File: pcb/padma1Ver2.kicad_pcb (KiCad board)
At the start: 2 copper layers, 33 x 68.6 mm, 15 parts, among them SW1 SPST

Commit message: added basic Pcb File
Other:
- board text added: "Padma1Ver2 - KSRMCE Kunchala Anil"
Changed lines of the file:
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@@
     (area 143.459999 81.229999 176.580001 149.910001)
     (thickness 1.6)
-    (drawings 7)
+    (drawings 8)
     (tracks 165)
     (zones 0)
@@
       (net 40 "Net-(R3-Pad1)"))
   )
+  (gr_text "Padma1Ver2 -  KSRMCE\nKunchala Anil" (at 166.37 83.185) (layer F.SilkS)
+    (effects (font (size 1 1) (thickness 0.25)))
+  )
   (gr_line (start 143.51 81.28) (end 143.51 82.55) (angle 90) (layer Edge.Cuts) (width 0.1))

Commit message: added ConfigJson Description file
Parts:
- D3: value LED_RCBG -> LED_RGB
- moved 10k1 3.17 mm to (150.5, 87.6)
- renumbered DTH1 to DTH, LDR1 to LDR, MOIS1 to SMS
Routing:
- net Net-(10k1-Pad2): track 39.1 -> 82.9 mm, vias 1 -> 3
- net Net-(10k1-Pad1): track 31.9 -> 61.9 mm
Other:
- board text added: "Padma1Ver2 - Innovation Lab"
- board text removed: "Padma1Ver2 - KSRMCE Kunchala Anil"
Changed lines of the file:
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@@
     (thickness 1.6)
     (drawings 8)
-    (tracks 165)
+    (tracks 186)
     (zones 0)
     (modules 15)
@@
     (visible_elements FFFFFF7F)
     (pcbplotparams
-      (layerselection 0x00030_80000001)
+      (layerselection 0x010f0_80000001)
       (usegerberextensions false)
       (excludeedgelayer true)
@@
       (outputformat 1)
       (mirror false)
-      (drillshape 1)
+      (drillshape 0)
       (scaleselection 1)
       (outputdirectory ""))
@@
   )
   (module Resistors_ThroughHole:Resistor_Horizontal_RM10mm placed (layer F.Cu)
-    (at 148.59 85.09)
+    (at 150.495 87.63)
     (descr "Resistor, Axial,  RM 10mm, 1/3W")
     (tags "Resistor Axial RM 10mm 1/3W")
@@
       (effects (font (size 1 1) (thickness 0.15)))
     )
-    (fp_text value LED_RCBG (at 3.175 1.27 540) (layer F.Fab)
+    (fp_text value LED_RGB (at 3.175 1.27 360) (layer F.Fab)
       (effects (font (size 1 1) (thickness 0.15)))
     )
@@
     (descr "Through hole pin header")
     (tags "pin header")
-    (fp_text reference DTH1 (at 3.175 3.81 90) (layer F.SilkS)
+    (fp_text reference DTH (at 3.175 3.81 90) (layer F.SilkS)
       (effects (font (size 1 1) (thickness 0.15)))
     )
@@
     (descr "Through hole pin header")
     (tags "pin header")
-    (fp_text reference LDR1 (at -2.54 3.81 270) (layer F.SilkS)
+    (fp_text reference LDR (at -2.54 3.81 270) (layer F.SilkS)
       (effects (font (size 1 1) (thickness 0.15)))
     )
@@
     (descr "Through hole pin header")
     (tags "pin header")
-    (fp_text reference MOIS1 (at 2.54 3.175 90) (layer F.SilkS)
+    (fp_text reference SMS (at 2.54 3.175 90) (layer F.SilkS)
       (effects (font (size 1 1) (thickness 0.15)))
     )
@@
       (net 40 "Net-(R3-Pad1)"))
   )
-  (gr_text "Padma1Ver2 -  KSRMCE\nKunchala Anil" (at 166.37 83.185) (layer F.SilkS)
+  (gr_text "Padma1Ver2 -  Innovation Lab\n" (at 162.56 82.55) (layer F.SilkS)
     (effects (font (size 1 1) (thickness 0.25)))
   )
@@
   (segment (start 170.18 106.045) (end 170.815 106.68) (width 0.25) (layer B.Cu) (net 2) (status 80000))
   (segment (start 170.815 106.68) (end 171.45 106.68) (width 0.25) (layer B.Cu) (net 2) (status 80000))
+  (segment (start 150.495 87.63) (end 151.13 88.265) (width 0.25) (layer F.Cu) (net 3) (status 80000))
+  (segment (start 151.13 88.265) (end 151.13 89.535) (width 0.25) (layer F.Cu) (net 3) (status 80000))
+  (segment (start 151.13 89.535) (end 153.035 91.44) (width 0.25) (layer F.Cu) (net 3) (status 80000))
+  (segment (start 153.035 91.44) (end 153.035 93.345) (width 0.25) (layer F.Cu) (net 3) (status 80000))
+  (segment (start 153.035 93.345) (end 154.305 94.615) (width 0.25) (layer F.Cu) (net 3) (status 80000))
+  (segment (start 154.305 94.615) (end 154.305 111.76) (width 0.25) (layer F.Cu) (net 3) (status 80000))
+  (segment (start 154.305 111.76) (end 156.845 111.76) (width 0.25) (layer F.Cu) (net 3) (status 80000))
+  (segment (start 156.845 111.76) (end 158.115 113.03) (width 0.25) (layer F.Cu) (net 3) (status 80000))
   (segment (start 148.59 85.09) (end 154.305 90.805) (width 0.25) (layer F.Cu) (net 3) (status 80000))
   (segment (start 154.305 90.805) (end 154.305 92.71) (width 0.25) (layer F.Cu) (net 3) (status 80000))
@@
   (segment (start 156.845 109.22) (end 158.115 110.49) (width 0.25) (layer F.Cu) (net 3) (status 80000))
   (segment (start 158.115 110.49) (end 158.115 113.03) (width 0.25) (layer F.Cu) (net 3) (status 80000))
+  (segment (start 168.275 114.935) (end 168.91 115.57) (width 0.25) (layer B.Cu) (net 4) (status 80000))
+  (segment (start 168.91 115.57) (end 173.355 115.57) (width 0.25) (layer B.Cu) (net 4) (status 80000))
+  (segment (start 173.355 115.57) (end 176.53 112.395) (width 0.25) (layer B.Cu) (net 4) (status 80000))
+  (via (at 176.53 112.395) (size 0.6) (layers F.Cu B.Cu) (net 4) (status 80000))
+  (segment (start 176.53 112.395) (end 175.895 111.76) (width 0.25) (layer F.Cu) (net 4) (status 80000))
+  (segment (start 175.895 111.76) (end 175.895 99.06) (width 0.25) (layer F.Cu) (net 4) (status 80000))
+  (via (at 175.895 99.06) (size 0.6) (layers F.Cu B.Cu) (net 4) (status 80000))
+  (segment (start 175.895 99.06) (end 174.625 97.79) (width 0.25) (layer B.Cu) (net 4) (status 80000))
+  (segment (start 174.625 97.79) (end 174.625 97.155) (width 0.25) (layer B.Cu) (net 4) (status 80000))
+  (segment (start 174.625 97.155) (end 170.815 97.155) (width 0.25) (layer B.Cu) (net 4) (status 80000))
+  (segment (start 170.815 97.155) (end 165.1 91.44) (width 0.25) (layer B.Cu) (net 4) (status 80000))
+  (segment (start 165.1 91.44) (end 164.465 91.44) (width 0.25) (layer B.Cu) (net 4) (status 80000))
+  (segment (start 164.465 91.44) (end 160.655 87.63) (width 0.25) (layer B.Cu) (net 4) (status 80000))
   (segment (start 168.275 114.935) (end 167.005 116.205) (width 0.25) (layer B.Cu) (net 4) (status 80000))
   (segment (start 167.005 116.205) (end 166.37 116.205) (width 0.25) (layer B.Cu) (net 4) (status 80000))

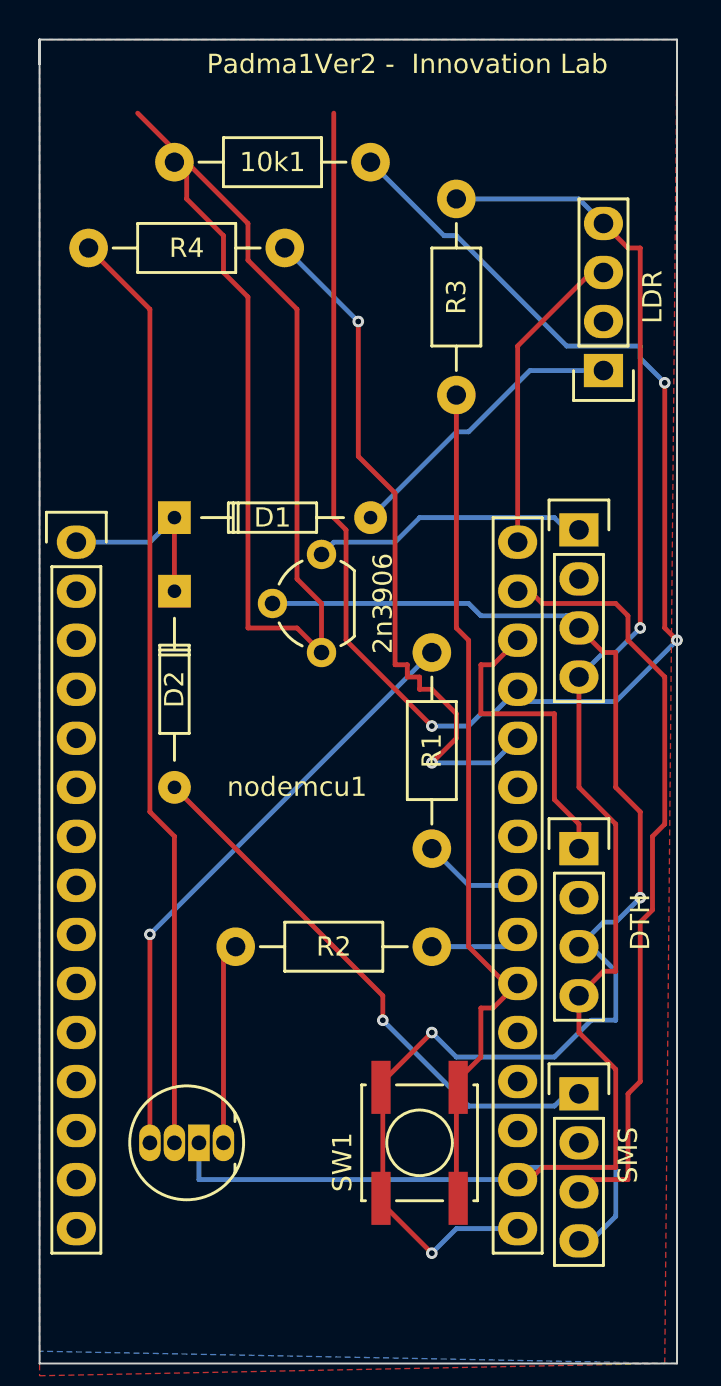
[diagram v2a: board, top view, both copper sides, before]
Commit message: added random clientid generator
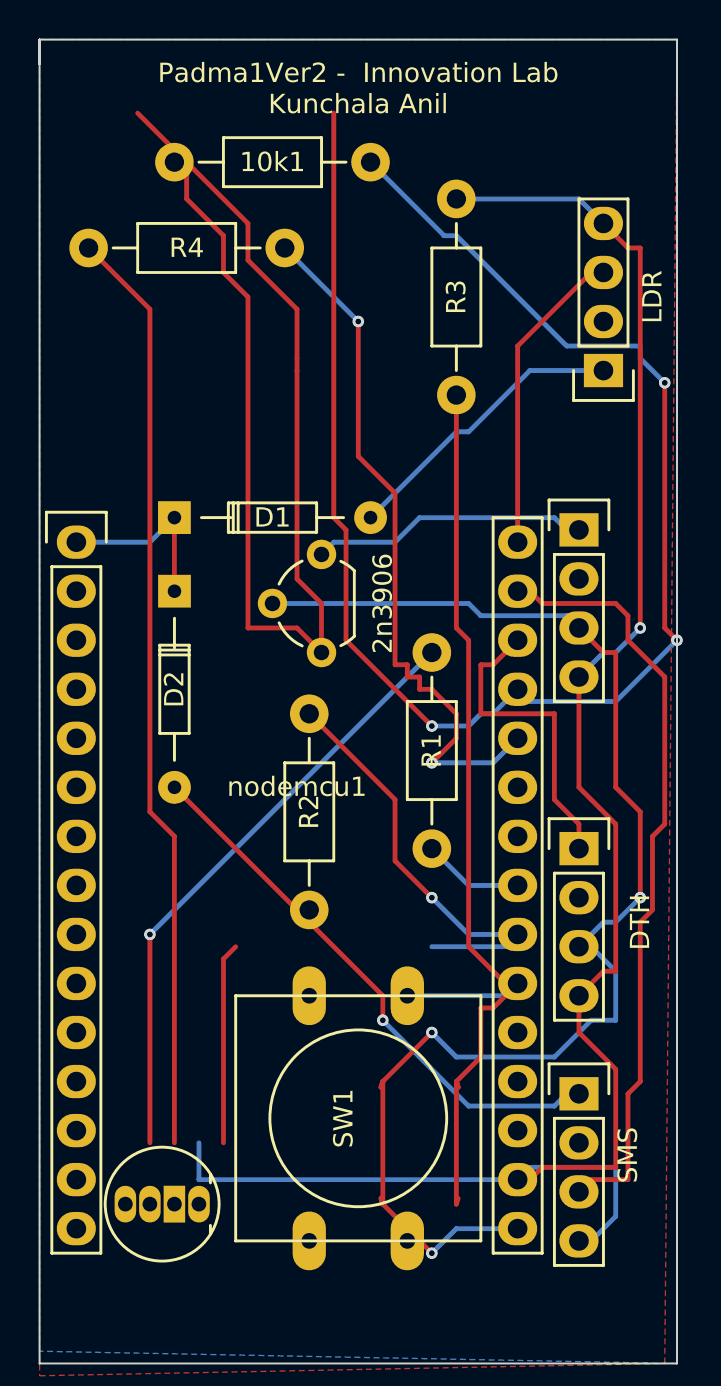
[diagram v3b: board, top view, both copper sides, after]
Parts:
- SW1: footprint Buttons_Switches_SMD:SW_SPST_EVPBF -> Buttons_Switches_ThroughHole:SW_PUSH-12mm
- moved R2 4.26 mm to (157.5, 126.4), turned to 90 degrees
- moved D3 3.42 mm to (151.8, 141.6)
- moved SW1 3.42 mm to (160.0, 137.2)
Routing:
- net Net-(R2-Pad2): track 4.71 -> 22.1 mm, vias 0 -> 1
- net Net-(D3-Pad1): track 10.4 -> 0.00 mm
- net (no net): track 0.00 -> 10.4 mm
- net Net-(R3-Pad1): track 46.2 -> 52.2 mm
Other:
- board text added: "Padma1Ver2 - Innovation Lab Kunchala Anil"
- board text removed: "Padma1Ver2 - Innovation Lab"

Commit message: pcb Without Any Errors
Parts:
- removed DTH, LDR, SMS: CONN_01X04, Pin_Headers:Pin_Header_Straight_1x04
- removed Grovr1: RLY, Pin_Headers:Pin_Header_Straight_1x04
- removed nodemcu1: nodemcu, nodemcu:NodeMCU_Amica_R2
- added DTH-SNPE: CONN_01X04, Terminal_Blocks:TerminalBlock_Pheonix_MKDS1.5-4pol, F.Cu at (128.5, 87.4)
- added LDR-SNPE: CONN_01X04, Terminal_Blocks:TerminalBlock_Pheonix_MKDS1.5-4pol, F.Cu at (106.2, 60.5)
- added MOIS-SNPE: CONN_01X04, Terminal_Blocks:TerminalBlock_Pheonix_MKDS1.5-4pol, F.Cu at (106.7, 121.9)
- added RLY-SNPE: RLY, Terminal_Blocks:TerminalBlock_Pheonix_MKDS1.5-4pol, F.Cu at (128.0, 112.3)
- added nodemcu: nodemcu, nodemcu:NodeMCU_Amica_R2, F.Cu at (76.9, 75.0)
- D3: value LED_RGB -> LED_RCBG; footprint LEDs:LED-RGB-5MM_Common_Cathode -> LED5_RGB:LED5_RGB_long_wide
- moved D1 82.7 mm to (81.8, 59.9)
- moved D2 82.6 mm to (81.8, 64.0), turned to 0 degrees
- moved R3 81.5 mm to (90.4, 67.1), turned to 0 degrees
- moved R4 79.1 mm to (83.8, 124.0), turned to 0 degrees
- moved SW1 73.8 mm to (111.8, 81.3), turned to 0 degrees
- moved R1 62.8 mm to (105.7, 99.6), turned to 0 degrees
- moved R2 61.6 mm to (105.7, 93.0), turned to 0 degrees
- moved D3 56.5 mm to (106.2, 108.2), turned to 0 degrees
- moved 2n3906 44.0 mm to (114.3, 108.7), turned to 0 degrees
- moved 10k1 38.4 mm to (116.3, 70.1), turned to 180 degrees
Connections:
- D1 pad 2: Net-(D1-Pad2) -> /signal
- D2 pad 2: Net-(D2-Pad2) -> /signal
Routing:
- net /signal: track 0.00 -> 117.0 mm
- net /power: track 0.00 -> 80.3 mm, vias 0 -> 1
- net Net-(10k1-Pad2): track 82.9 -> 16.0 mm, vias 3 -> 0
- net Net-(R3-Pad1): track 52.2 -> 117.8 mm, vias 0 -> 8
- net Net-(R4-Pad1): track 37.0 -> 88.7 mm
- net Earth: track 96.7 -> 146.4 mm, vias 1 -> 2
- net Net-(MOIS1-Pad3): track 39.8 -> 0.00 mm
- net Net-(D2-Pad2): track 28.8 -> 0.00 mm, vias 1 -> 0
- net Net-(D3-Pad3): track 48.2 -> 72.7 mm, vias 0 -> 3
- net Net-(10k1-Pad1): track 61.9 -> 40.7 mm
- net Net-(D3-Pad4): track 31.4 -> 11.2 mm, vias 1 -> 0
- net Net-(D3-Pad1): track 0.00 -> 16.8 mm
- net Net-(DTH1-Pad1): track 16.3 -> 0.00 mm
- net Net-(LDR1-Pad3): track 16.2 -> 0.00 mm
- net Net-(D1-Pad2): track 15.2 -> 0.00 mm
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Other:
- board size 33 x 68.6 mm -> 64.5 x 79.2 mm
- board text added: "Padma1Ver2 - Innovation Lab KSRMCE - KADAPA"
- board text removed: "Padma1Ver2 - Innovation Lab Kunchala Anil"
